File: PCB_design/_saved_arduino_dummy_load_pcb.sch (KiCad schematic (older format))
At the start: 22 parts, among them J1 Barrel_Jack, J2 Conn_02x08_Odd_Even, U1 MCP3208

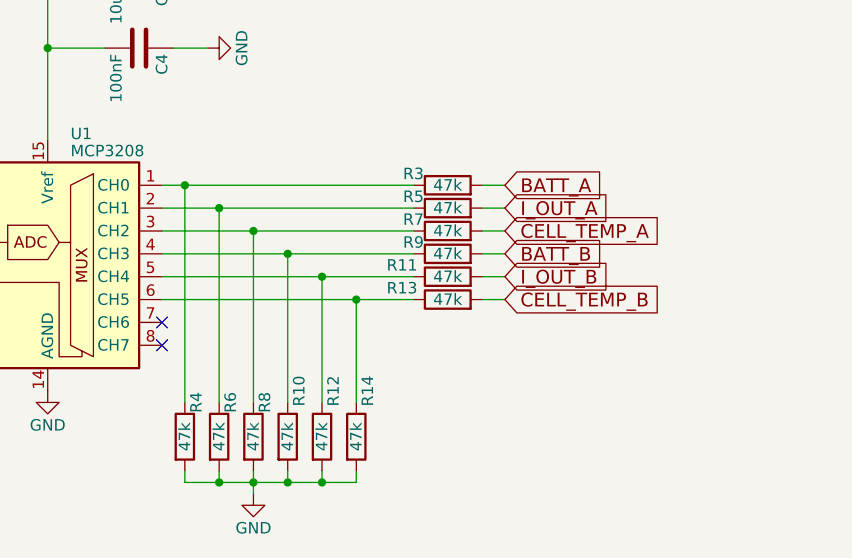
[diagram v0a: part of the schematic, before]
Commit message: nearly finished PCB layout and routing
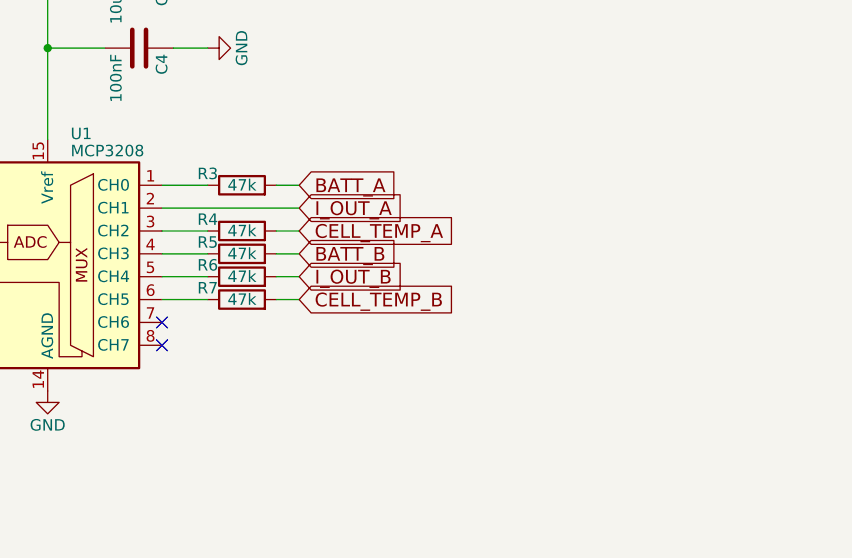
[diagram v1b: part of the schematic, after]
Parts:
- removed R10, R11, R12, R13, R14, R8, R9: 47k, Resistors_SMD:R_0805_HandSoldering, symbol R
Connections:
- net BATT_B: now also R5.2
- net CELL_TEMP_A: now also R4.2; no longer R7.2
- net CELL_TEMP_B: now also R7.2
- net GND: no longer R4.2, R6.2
- net I_OUT_A: now also U1.2 (CH1); no longer R5.2
- net I_OUT_B: now also R6.2
- net at R3.1, U1.1 (CH0): no longer R4.1
- net at U1.3 (CH2): now also R4.1; no longer R7.1
- net at U1.4 (CH3): now also R5.1
- net at U1.5 (CH4): now also R6.1
- net at U1.6 (CH5): now also R7.1
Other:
- moved on the sheet: R3, R4, R5, R6, R7
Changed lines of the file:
@@
 Text GLabel 2500 3250 2    60   Input ~ 0
 I_SET
-Text GLabel 5650 3150 2    60   Input ~ 0
+Text GLabel 4750 3150 2    60   Input ~ 0
 BATT_A
-Text GLabel 5650 3450 2    60   Input ~ 0
+Text GLabel 4750 3450 2    60   Input ~ 0
 BATT_B
 $Comp
@@
 	1    0    0    -1
 $EndComp
-Text GLabel 5650 3250 2    60   Input ~ 0
+Text GLabel 4750 3250 2    60   Input ~ 0
 I_OUT_A
 $Comp
 L R R3
 U 1 1 5A2169A9
-P 5400 3150
-F 0 "R3" V 5450 3300 50  0000 C CNN
-F 1 "47k" V 5400 3150 50  0000 C CNN
-F 2 "Resistors_SMD:R_0805_HandSoldering" V 5330 3150 50  0001 C CNN
-F 3 "" H 5400 3150 50  0001 C CNN
-	1    5400 3150
+P 4500 3150
+F 0 "R3" V 4550 3300 50  0000 C CNN
+F 1 "47k" V 4500 3150 50  0000 C CNN
+F 2 "Resistors_SMD:R_0805_HandSoldering" V 4430 3150 50  0001 C CNN
+F 3 "" H 4500 3150 50  0001 C CNN
+	1    4500 3150
 	0    -1   -1   0
 $EndComp
@@
 L R R4
 U 1 1 5A216AEF
-P 4250 4250
-F 0 "R4" V 4300 4400 50  0000 C CNN
-F 1 "47k" V 4250 4250 50  0000 C CNN
-F 2 "Resistors_SMD:R_0805_HandSoldering" V 4180 4250 50  0001 C CNN
-F 3 "" H 4250 4250 50  0001 C CNN
-	1    4250 4250
-	1    0    0    -1
+P 4500 3350
+F 0 "R4" V 4550 3500 50  0000 C CNN
+F 1 "47k" V 4500 3350 50  0000 C CNN
+F 2 "Resistors_SMD:R_0805_HandSoldering" V 4430 3350 50  0001 C CNN
+F 3 "" H 4500 3350 50  0001 C CNN
+	1    4500 3350
+	0    -1   -1   0
 $EndComp
 Text GLabel 2500 3150 2    60   Input ~ 0
@@
 L R R5
 U 1 1 5A22131E
-P 5400 3250
-F 0 "R5" V 5450 3400 50  0000 C CNN
-F 1 "47k" V 5400 3250 50  0000 C CNN
-F 2 "Resistors_SMD:R_0805_HandSoldering" V 5330 3250 50  0001 C CNN
-F 3 "" H 5400 3250 50  0001 C CNN
-	1    5400 3250
+P 4500 3450
+F 0 "R5" V 4550 3600 50  0000 C CNN
+F 1 "47k" V 4500 3450 50  0000 C CNN
+F 2 "Resistors_SMD:R_0805_HandSoldering" V 4430 3450 50  0001 C CNN
+F 3 "" H 4500 3450 50  0001 C CNN
+	1    4500 3450
 	0    -1   -1   0
 $EndComp
@@
 L R R7
 U 1 1 5A22951F
-P 5400 3350
-F 0 "R7" V 5450 3500 50  0000 C CNN
-F 1 "47k" V 5400 3350 50  0000 C CNN
-F 2 "Resistors_SMD:R_0805_HandSoldering" V 5330 3350 50  0001 C CNN
-F 3 "" H 5400 3350 50  0001 C CNN
-	1    5400 3350
+P 4500 3650
+F 0 "R7" V 4550 3800 50  0000 C CNN
+F 1 "47k" V 4500 3650 50  0000 C CNN
+F 2 "Resistors_SMD:R_0805_HandSoldering" V 4430 3650 50  0001 C CNN
+F 3 "" H 4500 3650 50  0001 C CNN
+	1    4500 3650
 	0    -1   -1   0
 $EndComp
@@
 L R R6
 U 1 1 5A2293D0
-P 4400 4250
-F 0 "R6" V 4450 4400 50  0000 C CNN
-F 1 "47k" V 4400 4250 50  0000 C CNN
-F 2 "Resistors_SMD:R_0805_HandSoldering" V 4330 4250 50  0001 C CNN
-F 3 "" H 4400 4250 50  0001 C CNN
-	1    4400 4250
-	1    0    0    -1
-$EndComp
-Text GLabel 5650 3350 2    60   Input ~ 0
+P 4500 3550
+F 0 "R6" V 4550 3700 50  0000 C CNN
+F 1 "47k" V 4500 3550 50  0000 C CNN
+F 2 "Resistors_SMD:R_0805_HandSoldering" V 4430 3550 50  0001 C CNN
+F 3 "" H 4500 3550 50  0001 C CNN
+	1    4500 3550
+	0    -1   -1   0
+$EndComp
+Text GLabel 4750 3350 2    60   Input ~ 0
 CELL_TEMP_A
-Text GLabel 5650 3650 2    60   Input ~ 0
+Text GLabel 4750 3650 2    60   Input ~ 0
 CELL_TEMP_B
-$Comp
-L R R8
-U 1 1 5A230070
-P 4550 4250
-F 0 "R8" V 4600 4400 50  0000 C CNN
-F 1 "47k" V 4550 4250 50  0000 C CNN
-F 2 "Resistors_SMD:R_0805_HandSoldering" V 4480 4250 50  0001 C CNN
-F 3 "" H 4550 4250 50  0001 C CNN
-	1    4550 4250
-	1    0    0    -1
-$EndComp
 $Comp
 L Conn_02x08_Odd_Even J2
@@
 $EndComp
 $Comp
-L GND #PWR06
-U 1 1 59F7608A
-P 4550 4500
-F 0 "#PWR06" H 4550 4250 50  0001 C CNN
-F 1 "GND" H 4550 4350 50  0000 C CNN
-F 2 "" H 4550 4500 50  0001 C CNN
-F 3 "" H 4550 4500 50  0001 C CNN
-	1    4550 4500
-	1    0    0    -1
-$EndComp
-$Comp
-L R R9
-U 1 1 59F777FF
-P 5400 3450
-F 0 "R9" V 5450 3600 50  0000 C CNN
-F 1 "47k" V 5400 3450 50  0000 C CNN
-F 2 "Resistors_SMD:R_0805_HandSoldering" V 5330 3450 50  0001 C CNN
-F 3 "" H 5400 3450 50  0001 C CNN
-	1    5400 3450
-	0    -1   -1   0
-$EndComp
-$Comp
-L R R10
-U 1 1 59F77966
-P 4700 4250
-F 0 "R10" V 4750 4450 50  0000 C CNN
-F 1 "47k" V 4700 4250 50  0000 C CNN
-F 2 "Resistors_SMD:R_0805_HandSoldering" V 4630 4250 50  0001 C CNN
-F 3 "" H 4700 4250 50  0001 C CNN
-	1    4700 4250
-	1    0    0    -1
-$EndComp
-$Comp
-L +5V #PWR07
+L +5V #PWR06
 U 1 1 59F7FE3E
 P 3350 2150
-F 0 "#PWR07" H 3350 2000 50  0001 C CNN
+F 0 "#PWR06" H 3350 2000 50  0001 C CNN
 F 1 "+5V" H 3350 2290 50  0000 C CNN
 F 2 "" H 3350 2150 50  0001 C CNN
@@
 $EndComp
 $Comp
-L GND #PWR08
+L GND #PWR07
 U 1 1 59F80B3F
 P 3350 4050
-F 0 "#PWR08" H 3350 3800 50  0001 C CNN
+F 0 "#PWR07" H 3350 3800 50  0001 C CNN
 F 1 "GND" H 3350 3900 50  0000 C CNN
 F 2 "" H 3350 4050 50  0001 C CNN
@@
 $EndComp
 $Comp
-L GND #PWR09
+L GND #PWR08
 U 1 1 59F80CA3
 P 2650 2250
-F 0 "#PWR09" H 2650 2000 50  0001 C CNN
+F 0 "#PWR08" H 2650 2000 50  0001 C CNN
 F 1 "GND" H 2650 2100 50  0000 C CNN
 F 2 "" H 2650 2250 50  0001 C CNN
@@
 $EndComp
 $Comp
-L GND #PWR010
+L GND #PWR09
 U 1 1 59FD1D7D
 P 4200 1450
-F 0 "#PWR010" H 4200 1200 50  0001 C CNN
+F 0 "#PWR09" H 4200 1200 50  0001 C CNN
 F 1 "GND" H 4200 1300 50  0000 C CNN
 F 2 "" H 4200 1450 50  0001 C CNN
@@
 Connection ~ 3000 1150
 Wire Wire Line
-	5550 3150 5650 3150
-Wire Wire Line
-	5550 3250 5650 3250
+	4650 3150 4750 3150
+Wire Wire Line
+	4150 3250 4750 3250
 Wire Wire Line
 	4200 1350 4200 1450
@@
 Connection ~ 1600 3750
 Wire Wire Line
-	5550 3350 5650 3350
+	4650 3350 4750 3350
 Wire Wire Line
 	1600 3150 1600 4000
@@
 	2500 3250 2450 3250
 Wire Wire Line
-	4150 3150 5250 3150
-Wire Wire Line
-	4150 3450 5250 3450
-Wire Wire Line
-	4150 3550 5250 3550
-Wire Wire Line
-	4150 3650 5250 3650
-Wire Wire Line
-	4150 3350 5250 3350
-Wire Wire Line
-	4150 3250 5250 3250
-Wire Wire Line
-	4250 4100 4250 3150
-Connection ~ 4250 3150
-Wire Wire Line
-	4400 4100 4400 3250
-Connection ~ 4400 3250
+	4150 3150 4350 3150
+Wire Wire Line
+	4150 3450 4350 3450
+Wire Wire Line
+	4150 3550 4350 3550
+Wire Wire Line
+	4150 3650 4350 3650
+Wire Wire Line
+	4150 3350 4350 3350
 Wire Wire Line
 	3350 2150 3350 2950
@@
 $EndComp
 NoConn ~ 2100 3850
-$Comp
-L R R11
-U 1 1 5A08A828
-P 5400 3550
-F 0 "R11" V 5450 3750 50  0000 C CNN
-F 1 "47k" V 5400 3550 50  0000 C CNN
-F 2 "Resistors_SMD:R_0805_HandSoldering" V 5330 3550 50  0001 C CNN
-F 3 "" H 5400 3550 50  0001 C CNN
-	1    5400 3550
-	0    -1   -1   0
-$EndComp
-$Comp
-L R R12
-U 1 1 5A08A8C0
-P 4850 4250
-F 0 "R12" V 4900 4450 50  0000 C CNN
-F 1 "47k" V 4850 4250 50  0000 C CNN
-F 2 "Resistors_SMD:R_0805_HandSoldering" V 4780 4250 50  0001 C CNN
-F 3 "" H 4850 4250 50  0001 C CNN
-	1    4850 4250
-	1    0    0    -1
-$EndComp
 Text GLabel 5750 1250 0    60   Input ~ 0
 CHARGE
@@
 	7300 1050 7200 1050
 Wire Wire Line
-	5550 3450 5650 3450
-Wire Wire Line
-	5650 3550 5550 3550
-Wire Wire Line
-	5550 3650 5650 3650
+	4650 3450 4750 3450
+Wire Wire Line
+	4750 3550 4650 3550
+Wire Wire Line
+	4650 3650 4750 3650
 $Sheet
 S 5850 1650 1350 450
@@
 Connection ~ 3650 2550
 $Comp
-L GND #PWR011
+L GND #PWR010
 U 1 1 5A04B5B5
 P 2650 2550
-F 0 "#PWR011" H 2650 2300 50  0001 C CNN
+F 0 "#PWR010" H 2650 2300 50  0001 C CNN
 F 1 "GND" H 2650 2400 50  0000 C CNN
 F 2 "" H 2650 2550 50  0001 C CNN
@@
 $EndComp
 $Comp
-L GND #PWR012
+L GND #PWR011
 U 1 1 5A04C217
 P 4350 2250
-F 0 "#PWR012" H 4350 2000 50  0001 C CNN
+F 0 "#PWR011" H 4350 2000 50  0001 C CNN
 F 1 "GND" H 4350 2100 50  0000 C CNN
 F 2 "" H 4350 2250 50  0001 C CNN
@@
 	3900 2550 3650 2550
 $Comp
-L GND #PWR013
+L GND #PWR012
 U 1 1 5A04CF95
 P 4350 2550
-F 0 "#PWR013" H 4350 2300 50  0001 C CNN
+F 0 "#PWR012" H 4350 2300 50  0001 C CNN
 F 1 "GND" H 4350 2400 50  0000 C CNN
 F 2 "" H 4350 2550 50  0001 C CNN
@@
 	4200 2550 4350 2550
 Connection ~ 3350 2550
-Text GLabel 5650 3550 2    60   Input ~ 0
+Text GLabel 4750 3550 2    60   Input ~ 0
 I_OUT_B
-Wire Wire Line
-	4250 4400 4250 4450
-Wire Wire Line
-	4250 4450 5000 4450
-Wire Wire Line
-	4550 4400 4550 4500
-Wire Wire Line
-	4400 4400 4400 4450
-Connection ~ 4400 4450
-Connection ~ 4550 4450
-Wire Wire Line
-	4700 4450 4700 4400
-Wire Wire Line
-	4850 4450 4850 4400
-Connection ~ 4700 4450
-Wire Wire Line
-	4550 4100 4550 3350
-Connection ~ 4550 3350
-Wire Wire Line
-	4700 4100 4700 3450
-Connection ~ 4700 3450
-Wire Wire Line
-	4850 4100 4850 3550
-Connection ~ 4850 3550
-$Comp
-L R R13
-U 1 1 5A066B2C
-P 5400 3650
-F 0 "R13" V 5450 3850 50  0000 C CNN
-F 1 "47k" V 5400 3650 50  0000 C CNN
-F 2 "Resistors_SMD:R_0805_HandSoldering" V 5330 3650 50  0001 C CNN
-F 3 "" H 5400 3650 50  0001 C CNN
-	1    5400 3650
-	0    -1   -1   0
-$EndComp
-$Comp
-L R R14
-U 1 1 5A066D11
-P 5000 4250
-F 0 "R14" V 5050 4450 50  0000 C CNN
-F 1 "47k" V 5000 4250 50  0000 C CNN
-F 2 "Resistors_SMD:R_0805_HandSoldering" V 4930 4250 50  0001 C CNN
-F 3 "" H 5000 4250 50  0001 C CNN
-	1    5000 4250
-	1    0    0    -1
-$EndComp
-Wire Wire Line
-	5000 4450 5000 4400
-Connection ~ 4850 4450
-Wire Wire Line
-	5000 4100 5000 3650
-Connection ~ 5000 3650
 NoConn ~ 4150 3750
 NoConn ~ 4150 3850

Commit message: Finalized/finished PCB layout. Phew! Version 0.00. Hopefully it works (fingers crossed)!
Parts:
- removed R6: 47k, Resistors_SMD:R_0805_HandSoldering, symbol R
- REG1: footprint (none) -> Library:LM2596_module
- renumbered R7 to R6
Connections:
- net I_OUT_B: now also U1.5 (CH4)
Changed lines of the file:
@@
 F 0 "REG1" H 3650 1000 60  0000 C CNN
 F 1 "REG" H 3650 1500 60  0000 C CNN
-F 2 "" H 3600 1250 60  0001 C CNN
+F 2 "Library:LM2596_module" H 3600 1250 60  0001 C CNN
 F 3 "" H 3600 1250 60  0001 C CNN
 	1    3650 1250
@@
 $EndComp
 $Comp
-L R R7
+L R R6
 U 1 1 5A22951F
 P 4500 3650
-F 0 "R7" V 4550 3800 50  0000 C CNN
+F 0 "R6" V 4550 3800 50  0000 C CNN
 F 1 "47k" V 4500 3650 50  0000 C CNN
 F 2 "Resistors_SMD:R_0805_HandSoldering" V 4430 3650 50  0001 C CNN
 F 3 "" H 4500 3650 50  0001 C CNN
 	1    4500 3650
-	0    -1   -1   0
-$EndComp
-$Comp
-L R R6
-U 1 1 5A2293D0
-P 4500 3550
-F 0 "R6" V 4550 3700 50  0000 C CNN
-F 1 "47k" V 4500 3550 50  0000 C CNN
-F 2 "Resistors_SMD:R_0805_HandSoldering" V 4430 3550 50  0001 C CNN
-F 3 "" H 4500 3550 50  0001 C CNN
-	1    4500 3550
 	0    -1   -1   0
 $EndComp
@@
 	4150 3450 4350 3450
 Wire Wire Line
-	4150 3550 4350 3550
+	4150 3550 4750 3550
 Wire Wire Line
 	4150 3650 4350 3650
@@
 	4650 3450 4750 3450
 Wire Wire Line
-	4750 3550 4650 3550
-Wire Wire Line
 	4650 3650 4750 3650
